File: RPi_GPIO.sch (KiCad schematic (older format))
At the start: 1 part, among them J2 RPi_GPIO

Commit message: First ver of schems
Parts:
- added C? (x9): 0.1uF, symbol Device:C
- added C?: C, symbol Device:C
- added D? (x5): LED, symbol Device:LED
- added J? (x4): Conn_01x03_Male, symbol Connector:Conn_01x03_Male
- added R? (x5): 180R, symbol Device:R
- added R? (x2): 10k, symbol Device:R
- added SW?: SW_Push, symbol Switch:SW_Push
- added U?: STM32F030CCTx, Package_QFP:LQFP-48_7x7mm_P0.5mm, symbol MCU_ST_STM32F0:STM32F030CCTx
- added U? (x4): MAX485E, symbol Interface_UART:MAX485E
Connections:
- net +3V3: now reaches J2.1 (3.3V)
- net +3V3: now also C?.1, C?.1, C?.1, C?.1, C?.1, C?.1, C?.1, C?.1, C?.1, R?.1, R?.1, U?.1 (VDD), U?.24 (VDD), U?.36 (VDD), U?.48 (VDD), U?.8 (VCC), U?.8 (VCC), U?.8 (VCC), U?.8 (VCC), U?.9 (VDDA)
- net GND: now reaches J2.14 (GND)
- net GND: now also J2.20 (GND), J2.25 (GND), J2.30 (GND), J2.34 (GND), J2.39 (GND), J2.6 (GND), J2.9 (GND), C?.2, C?.2, C?.2, C?.2, C?.2, D?.1 (K), D?.1 (K), D?.1 (K), D?.1 (K), D?.1 (K), J?.1 (Pin_1), J?.1 (Pin_1), J?.1 (Pin_1), J?.1 (Pin_1), R?.2, SW?.1, U?.23 (VSS), U?.35 (VSS), U?.47 (VSS), U?.5 (GND), U?.5 (GND), U?.5 (GND), U?.5 (GND), U?.8 (VSSA)
- net MOSI: now reaches J2.19 (BCM10_MOSI)
- net MOSI: now also U?.28 (PB15)
- net +5V: now reaches J2.2 (5V)
- net +5V: now also J2.4 (5V)
- net MISO: now reaches J2.21 (BCM9_MISO)
- net MISO: now also U?.27 (PB14)
- net SCLK: now reaches J2.23 (BCM11_SCLK)
- net SCLK: now also U?.26 (PB13)
- new net: C?.2, C?.2, C?.2, C?.2, C?.2
- new net: D?.2 (A), R?.2 (x5)
- new net: J?.2 (Pin_2), U?.6 (A) (x4)
- new net: J?.3 (Pin_3), U?.7 (B) (x4)
- new net BOOT0: R?.1, U?.44 (BOOT0)
- new net PB0: R?.1, U?.18 (PB0)
- new net PB1: R?.1, U?.19 (PB1)
- new net PB2: R?.1, U?.20 (PB2)
- new net PB3: R?.1, U?.39 (PB3)
- new net RESET: C?.1, R?.2, SW?.2, U?.7 (NRST)
- new net USART1_RX: U?.31 (PA10)
- new net USART1_TX: U?.30 (PA9)
- new net USART2_RX: U?.1 (RO), U?.13 (PA3)
- new net USART2_TX: U?.12 (PA2), U?.4 (DI)
- new net USART3_RX: U?.1 (RO), U?.22 (PB11)
- new net USART3_TX: U?.21 (PB10), U?.4 (DI)
- new net USART4_RX: U?.1 (RO), U?.11 (PA1)
- new net USART4_TX: U?.10 (PA0), U?.4 (DI)
- new net USART6_RX: U?.1 (RO), U?.15 (PA5)
- new net USART6_TX: U?.14 (PA4), U?.4 (DI)
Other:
- note added: "BOOT0 -> 0 : boot from flash"
- note added: "Decoupling capacitors for stm32\n"
- moved on the sheet: J2

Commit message: Improve schems
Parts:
- removed R?: 10k, symbol Device:R
- added 8MHz1: Crystal, symbol Device:Crystal
- added C11, C12: 20pF, symbol Device:C
- added J3: Conn_02x03_Counter_Clockwise, symbol Connector_Generic:Conn_02x03_Counter_Clockwise
- added J4: Conn_01x02_Male, symbol Connector:Conn_01x02_Male
- added R7: 560, symbol Device:R
- added R8: 10k, symbol Device:R
- C8: renamed from C?; value C -> 100nF
- D1: renamed from D?; footprint (none) -> LEDs:LED_0603_HandSoldering; dkReference (none) -> 160-1446-1-ND
- D2, D3, D4, D5: renamed from D?; footprint (none) -> LEDs:LED_0603_HandSoldering; dkReference (none) -> SML-D12U1WT86CT-ND
- U2: renamed from U?; dkReference (none) -> 497-17296-ND
- U3, U4, U5, U6: renamed from U?; dkReference (none) -> MAX485ESA+-ND
- gave numbers to parts that had none: 20
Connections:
- net +3V3: now also J3.1 (Pin_1), R8.1
- net +5V: now also J3.6 (Pin_6)
- net BOOT0: now also R7.2
- net GND: now also C11.1, C12.1, J3.4 (Pin_4), J4.1 (Pin_1)
- net RESET: now also J3.5 (Pin_5)
- net SWDIO: now reaches U2.34 (PA13)
- net SWDIO: now also J3.3 (Pin_3)
- net SWCLK: now reaches U2.37 (PA14)
- net SWCLK: now also J3.2 (Pin_2)
- net OSC_IN: now reaches U2.5 (PF0)
- net OSC_OUT: now reaches U2.6 (PF1)
- new net: J4.2 (Pin_2), R7.1, R8.2
- new net: 8MHz1.1, C11.2
- new net: 8MHz1.2, C12.2
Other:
- moved on the sheet: J2

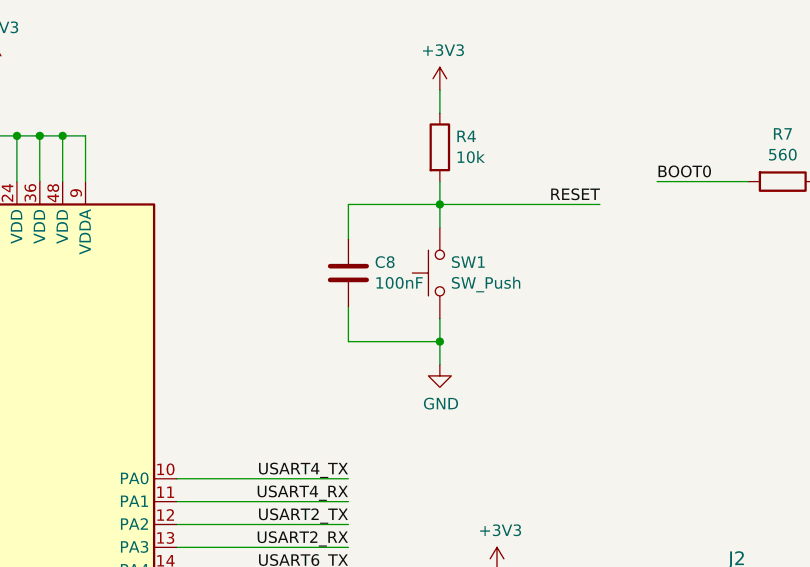
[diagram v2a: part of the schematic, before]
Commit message: Start to fill components footprints and dkRef
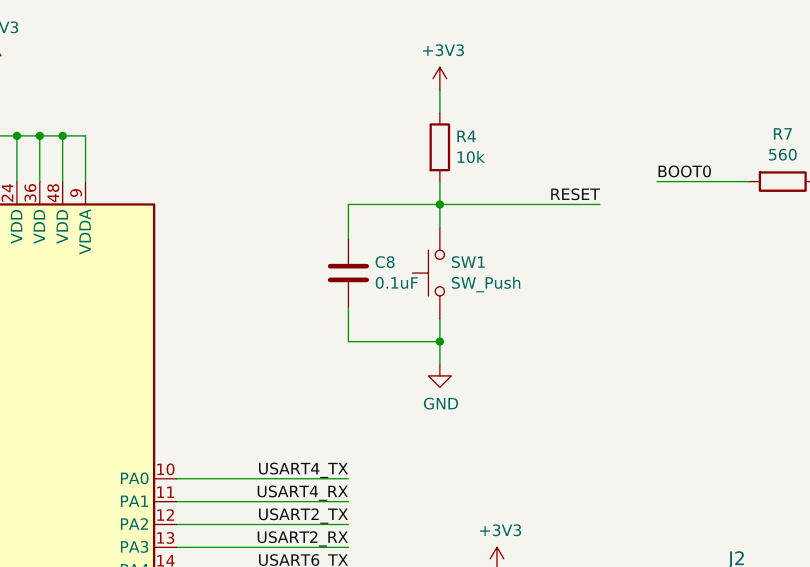
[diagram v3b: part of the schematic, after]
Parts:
- 8MHz1: footprint (none) -> Crystals:Crystal_SMD_HC49-SD_HandSoldering; dkReference (none) -> 535-10212-1-ND
- C10, C13, C14, C3, C4, C5, C6, C7, C9: footprint (none) -> Capacitors_SMD:C_0603_HandSoldering; dkReference (none) -> 1276-6439-1-ND
- C8: value 100nF -> 0.1uF; footprint (none) -> Capacitors_SMD:C_0603_HandSoldering; dkReference (none) -> 1276-6439-1-ND
- SW1: footprint (none) -> digikey-footprints:Switch_Tactile_SMD_6x6mm; dkReference (none) -> 486-3690-ND
- U3, U4, U5, U6: footprint (none) -> digikey-footprints:SOIC-8_W3.9mm
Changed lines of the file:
@@
 F 0 "C3" H 1115 1496 50  0000 L CNN
 F 1 "0.1uF" H 1050 1350 50  0000 L CNN
-F 2 "" H 1038 1300 50  0001 C CNN
+F 2 "Capacitors_SMD:C_0603_HandSoldering" H 1038 1300 50  0001 C CNN
 F 3 "~" H 1000 1450 50  0001 C CNN
+F 4 "1276-6439-1-ND" H 1000 1450 50  0001 C CNN "dkReference"
 	1    1000 1450
 	1    0    0    -1
@@
 F 0 "C4" H 1465 1496 50  0000 L CNN
 F 1 "0.1uF" H 1400 1350 50  0000 L CNN
-F 2 "" H 1388 1300 50  0001 C CNN
+F 2 "Capacitors_SMD:C_0603_HandSoldering" H 1388 1300 50  0001 C CNN
 F 3 "~" H 1350 1450 50  0001 C CNN
+F 4 "1276-6439-1-ND" H 1350 1450 50  0001 C CNN "dkReference"
 	1    1350 1450
 	1    0    0    -1
@@
 F 0 "C5" H 1815 1496 50  0000 L CNN
 F 1 "0.1uF" H 1750 1350 50  0000 L CNN
-F 2 "" H 1738 1300 50  0001 C CNN
+F 2 "Capacitors_SMD:C_0603_HandSoldering" H 1738 1300 50  0001 C CNN
 F 3 "~" H 1700 1450 50  0001 C CNN
+F 4 "1276-6439-1-ND" H 1700 1450 50  0001 C CNN "dkReference"
 	1    1700 1450
 	1    0    0    -1
@@
 F 0 "C6" H 2165 1496 50  0000 L CNN
 F 1 "0.1uF" H 2100 1350 50  0000 L CNN
-F 2 "" H 2088 1300 50  0001 C CNN
+F 2 "Capacitors_SMD:C_0603_HandSoldering" H 2088 1300 50  0001 C CNN
 F 3 "~" H 2050 1450 50  0001 C CNN
+F 4 "1276-6439-1-ND" H 2050 1450 50  0001 C CNN "dkReference"
 	1    2050 1450
 	1    0    0    -1
@@
 F 0 "C7" H 2515 1496 50  0000 L CNN
 F 1 "0.1uF" H 2450 1350 50  0000 L CNN
-F 2 "" H 2438 1300 50  0001 C CNN
+F 2 "Capacitors_SMD:C_0603_HandSoldering" H 2438 1300 50  0001 C CNN
 F 3 "~" H 2400 1450 50  0001 C CNN
+F 4 "1276-6439-1-ND" H 2400 1450 50  0001 C CNN "dkReference"
 	1    2400 1450
 	1    0    0    -1
@@
 F 0 "SW1" V 4196 3752 50  0000 R CNN
 F 1 "SW_Push" V 4105 3752 50  0000 R CNN
-F 2 "" H 4150 4000 50  0001 C CNN
+F 2 "digikey-footprints:Switch_Tactile_SMD_6x6mm" H 4150 4000 50  0001 C CNN
 F 3 "" H 4150 4000 50  0001 C CNN
+F 4 "486-3690-ND" V 4150 3800 50  0001 C CNN "dkReference"
 	1    4150 3800
 	0    -1   -1   0
@@
 P 3750 3800
 F 0 "C8" H 3865 3846 50  0000 L CNN
-F 1 "100nF" H 3865 3755 50  0000 L CNN
-F 2 "" H 3788 3650 50  0001 C CNN
+F 1 "0.1uF" H 3865 3755 50  0000 L CNN
+F 2 "Capacitors_SMD:C_0603_HandSoldering" H 3788 3650 50  0001 C CNN
 F 3 "~" H 3750 3800 50  0001 C CNN
+F 4 "1276-6439-1-ND" H 3750 3800 50  0001 C CNN "dkReference"
 	1    3750 3800
 	1    0    0    -1
@@
 F 0 "U3" H 6750 2550 50  0000 C CNN
 F 1 "MAX485E" H 6750 2450 50  0000 C CNN
-F 2 "" H 7100 1200 50  0001 C CNN
+F 2 "digikey-footprints:SOIC-8_W3.9mm" H 7100 1200 50  0001 C CNN
 F 3 "https://datasheets.maximintegrated.com/en/ds/MAX1487E-MAX491E.pdf" H 7100 1950 50  0001 C CNN
 F 4 "MAX485ESA+-ND" H 7100 1900 50  0001 C CNN "dkReference"
@@
 F 0 "C9" H 7515 1146 50  0000 L CNN
 F 1 "0.1uF" H 7515 1055 50  0000 L CNN
-F 2 "" H 7438 950 50  0001 C CNN
+F 2 "Capacitors_SMD:C_0603_HandSoldering" H 7438 950 50  0001 C CNN
 F 3 "~" H 7400 1100 50  0001 C CNN
+F 4 "1276-6439-1-ND" H 7400 1100 50  0001 C CNN "dkReference"
 	1    7400 1100
 	1    0    0    -1
@@
 F 0 "U5" H 9200 2550 50  0000 C CNN
 F 1 "MAX485E" H 9200 2450 50  0000 C CNN
-F 2 "" H 9550 1200 50  0001 C CNN
+F 2 "digikey-footprints:SOIC-8_W3.9mm" H 9550 1200 50  0001 C CNN
 F 3 "https://datasheets.maximintegrated.com/en/ds/MAX1487E-MAX491E.pdf" H 9550 1950 50  0001 C CNN
 F 4 "MAX485ESA+-ND" H 9550 1900 50  0001 C CNN "dkReference"
@@
 F 0 "C13" H 9965 1146 50  0000 L CNN
 F 1 "0.1uF" H 9965 1055 50  0000 L CNN
-F 2 "" H 9888 950 50  0001 C CNN
+F 2 "Capacitors_SMD:C_0603_HandSoldering" H 9888 950 50  0001 C CNN
 F 3 "~" H 9850 1100 50  0001 C CNN
+F 4 "1276-6439-1-ND" H 9850 1100 50  0001 C CNN "dkReference"
 	1    9850 1100
 	1    0    0    -1
@@
 F 0 "U4" H 6750 4900 50  0000 C CNN
 F 1 "MAX485E" H 6750 4800 50  0000 C CNN
-F 2 "" H 7100 3550 50  0001 C CNN
+F 2 "digikey-footprints:SOIC-8_W3.9mm" H 7100 3550 50  0001 C CNN
 F 3 "https://datasheets.maximintegrated.com/en/ds/MAX1487E-MAX491E.pdf" H 7100 4300 50  0001 C CNN
 F 4 "MAX485ESA+-ND" H 7100 4250 50  0001 C CNN "dkReference"
@@
 F 0 "C10" H 7515 3496 50  0000 L CNN
 F 1 "0.1uF" H 7515 3405 50  0000 L CNN
-F 2 "" H 7438 3300 50  0001 C CNN
+F 2 "Capacitors_SMD:C_0603_HandSoldering" H 7438 3300 50  0001 C CNN
 F 3 "~" H 7400 3450 50  0001 C CNN
+F 4 "1276-6439-1-ND" H 7400 3450 50  0001 C CNN "dkReference"
 	1    7400 3450
 	1    0    0    -1
@@
 F 0 "U6" H 9200 4900 50  0000 C CNN
 F 1 "MAX485E" H 9200 4800 50  0000 C CNN
-F 2 "" H 9550 3550 50  0001 C CNN
+F 2 "digikey-footprints:SOIC-8_W3.9mm" H 9550 3550 50  0001 C CNN
 F 3 "https://datasheets.maximintegrated.com/en/ds/MAX1487E-MAX491E.pdf" H 9550 4300 50  0001 C CNN
 F 4 "MAX485ESA+-ND" H 9550 4250 50  0001 C CNN "dkReference"
@@
 F 0 "C14" H 9965 3496 50  0000 L CNN
 F 1 "0.1uF" H 9965 3405 50  0000 L CNN
-F 2 "" H 9888 3300 50  0001 C CNN
+F 2 "Capacitors_SMD:C_0603_HandSoldering" H 9888 3300 50  0001 C CNN
 F 3 "~" H 9850 3450 50  0001 C CNN
+F 4 "1276-6439-1-ND" H 9850 3450 50  0001 C CNN "dkReference"
 	1    9850 3450
 	1    0    0    -1
@@
 F 0 "8MHz1" V 8404 6081 50  0000 L CNN
 F 1 "Crystal" V 8495 6081 50  0000 L CNN
-F 2 "" H 8450 5950 50  0001 C CNN
+F 2 "Crystals:Crystal_SMD_HC49-SD_HandSoldering" H 8450 5950 50  0001 C CNN
 F 3 "~" H 8450 5950 50  0001 C CNN
+F 4 "535-10212-1-ND" V 8450 5950 50  0001 C CNN "dkReference"
 	1    8450 5950
 	0    1    1    0

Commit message: Change components ref and package
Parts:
- C11, C12: footprint (none) -> Capacitors_SMD:C_0603_HandSoldering; dkReference (none) -> 490-11315-1-ND
- J2: dkReference (none) -> SAM11959-ND
- J4, J5, J6, J7, J8: dkReference (none) -> ED2819-ND
- R1, R2, R3, R5, R6: footprint (none) -> Resistors_SMD:R_0603_HandSoldering; dkReference (none) -> YAG2450CT-ND
- R4, R8: footprint (none) -> Resistors_SMD:R_0603_HandSoldering; dkReference (none) -> RMCF0201FT10K0CT-ND
- R7: footprint (none) -> LEDs:LED_0603_HandSoldering; dkReference (none) -> RC0201JR-07560RL
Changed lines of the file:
@@
 F 2 "RPi_Hat:Pin_Header_Straight_2x20" H 4700 5300 60  0001 C CNN
 F 3 "" H 4700 5300 60  0000 C CNN
+F 4 "SAM11959-ND" H 0   0   50  0001 C CNN "dkReference"
 	1    4700 5300
 	1    0    0    -1
@@
 F 0 "R1" H 3170 1296 50  0000 L CNN
 F 1 "180R" H 3170 1205 50  0000 L CNN
-F 2 "" V 3030 1250 50  0001 C CNN
+F 2 "Resistors_SMD:R_0603_HandSoldering" V 3030 1250 50  0001 C CNN
 F 3 "~" H 3100 1250 50  0001 C CNN
+F 4 "YAG2450CT-ND" H 3100 1250 50  0001 C CNN "dkReference"
 	1    3100 1250
 	1    0    0    -1
@@
 F 0 "R4" H 4220 3296 50  0000 L CNN
 F 1 "10k" H 4220 3205 50  0000 L CNN
-F 2 "" V 4080 3250 50  0001 C CNN
+F 2 "Resistors_SMD:R_0603_HandSoldering" V 4080 3250 50  0001 C CNN
 F 3 "~" H 4150 3250 50  0001 C CNN
+F 4 "RMCF0201FT10K0CT-ND" H 4150 3250 50  0001 C CNN "dkReference"
 	1    4150 3250
 	1    0    0    -1
@@
 F 0 "R2" H 3570 1296 50  0000 L CNN
 F 1 "180R" H 3570 1205 50  0000 L CNN
-F 2 "" V 3430 1250 50  0001 C CNN
+F 2 "Resistors_SMD:R_0603_HandSoldering" V 3430 1250 50  0001 C CNN
 F 3 "~" H 3500 1250 50  0001 C CNN
+F 4 "YAG2450CT-ND" H 3500 1250 50  0001 C CNN "dkReference"
 	1    3500 1250
 	1    0    0    -1
@@
 F 0 "R3" H 3970 1296 50  0000 L CNN
 F 1 "180R" H 3970 1205 50  0000 L CNN
-F 2 "" V 3830 1250 50  0001 C CNN
+F 2 "Resistors_SMD:R_0603_HandSoldering" V 3830 1250 50  0001 C CNN
 F 3 "~" H 3900 1250 50  0001 C CNN
+F 4 "YAG2450CT-ND" H 3900 1250 50  0001 C CNN "dkReference"
 	1    3900 1250
 	1    0    0    -1
@@
 F 0 "R5" H 4370 1296 50  0000 L CNN
 F 1 "180R" H 4370 1205 50  0000 L CNN
-F 2 "" V 4230 1250 50  0001 C CNN
+F 2 "Resistors_SMD:R_0603_HandSoldering" V 4230 1250 50  0001 C CNN
 F 3 "~" H 4300 1250 50  0001 C CNN
+F 4 "YAG2450CT-ND" H 4300 1250 50  0001 C CNN "dkReference"
 	1    4300 1250
 	1    0    0    -1
@@
 F 0 "R6" H 4770 1296 50  0000 L CNN
 F 1 "180R" H 4770 1205 50  0000 L CNN
-F 2 "" V 4630 1250 50  0001 C CNN
+F 2 "Resistors_SMD:R_0603_HandSoldering" V 4630 1250 50  0001 C CNN
 F 3 "~" H 4700 1250 50  0001 C CNN
+F 4 "YAG2450CT-ND" H 4700 1250 50  0001 C CNN "dkReference"
 	1    4700 1250
 	1    0    0    -1
@@
 F 2 "" H 8200 1900 50  0001 C CNN
 F 3 "~" H 8200 1900 50  0001 C CNN
+F 4 "ED2819-ND" H 0   0   50  0001 C CNN "dkReference"
 	1    8200 1900
 	-1   0    0    1
@@
 F 2 "" H 10650 1900 50  0001 C CNN
 F 3 "~" H 10650 1900 50  0001 C CNN
+F 4 "ED2819-ND" H 0   0   50  0001 C CNN "dkReference"
 	1    10650 1900
 	-1   0    0    1
@@
 F 2 "" H 8200 4250 50  0001 C CNN
 F 3 "~" H 8200 4250 50  0001 C CNN
+F 4 "ED2819-ND" H 0   0   50  0001 C CNN "dkReference"
 	1    8200 4250
 	-1   0    0    1
@@
 F 2 "" H 10650 4250 50  0001 C CNN
 F 3 "~" H 10650 4250 50  0001 C CNN
+F 4 "ED2819-ND" H 0   0   50  0001 C CNN "dkReference"
 	1    10650 4250
 	-1   0    0    1
@@
 F 0 "R8" H 5970 3096 50  0000 L CNN
 F 1 "10k" H 5970 3005 50  0000 L CNN
-F 2 "" V 5830 3050 50  0001 C CNN
+F 2 "Resistors_SMD:R_0603_HandSoldering" V 5830 3050 50  0001 C CNN
 F 3 "~" H 5900 3050 50  0001 C CNN
+F 4 "RMCF0201FT10K0CT-ND" H 5900 3050 50  0001 C CNN "dkReference"
 	1    5900 3050
 	1    0    0    -1
@@
 F 0 "C11" V 8598 5700 50  0000 C CNN
 F 1 "20pF" V 8689 5700 50  0000 C CNN
-F 2 "" H 8888 5550 50  0001 C CNN
+F 2 "Capacitors_SMD:C_0603_HandSoldering" H 8888 5550 50  0001 C CNN
 F 3 "~" H 8850 5700 50  0001 C CNN
+F 4 "490-11315-1-ND" V 8850 5700 50  0001 C CNN "dkReference"
 	1    8850 5700
 	0    1    1    0
@@
 F 0 "C12" V 9100 6200 50  0000 C CNN
 F 1 "20pF" V 9000 6200 50  0000 C CNN
-F 2 "" H 8888 6050 50  0001 C CNN
+F 2 "Capacitors_SMD:C_0603_HandSoldering" H 8888 6050 50  0001 C CNN
 F 3 "~" H 8850 6200 50  0001 C CNN
+F 4 "490-11315-1-ND" V 8850 6200 50  0001 C CNN "dkReference"
 	1    8850 6200
 	0    1    1    0
@@
 F 2 "" H 6250 3500 50  0001 C CNN
 F 3 "~" H 6250 3500 50  0001 C CNN
+F 4 "ED2819-ND" H 0   0   50  0001 C CNN "dkReference"
 	1    6250 3500
 	-1   0    0    1
@@
 F 0 "R7" V 5443 3400 50  0000 C CNN
 F 1 "560" V 5534 3400 50  0000 C CNN
-F 2 "" V 5580 3400 50  0001 C CNN
+F 2 "LEDs:LED_0603_HandSoldering" V 5580 3400 50  0001 C CNN
 F 3 "~" H 5650 3400 50  0001 C CNN
+F 4 "RC0201JR-07560RL" V 5650 3400 50  0001 C CNN "dkReference"
 	1    5650 3400
 	0    1    1    0
